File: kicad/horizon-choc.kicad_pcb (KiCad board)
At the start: 2 copper layers, 252 x 68 mm, 117 parts, among them SW1 SW_Push, SW10 SW_Push, SW11 SW_Push, SW12 SW_Push, SW13 SW_Push, SW14 SW_Push, SW15 SW_Push, SW16 SW_Push, SW17 SW_Push, SW18 SW_Push, SW19 SW_Push, SW2 SW_Push, SW20 SW_Push, SW21 SW_Push, SW22 SW_Push, SW23 SW_Push, SW24 SW_Push, SW25 SW_Push, SW26 SW_Push, SW27 SW_Push, SW28 SW_Push, SW29 SW_Push, SW3 SW_Push, SW30 SW_Push, SW31 SW_Push, SW32 SW_Push, SW33 SW_Push, SW34 SW_Push, SW35 SW_Push, SW36 SW_Push, SW37 SW_Push, SW38 SW_Push, SW39 SW_Push, SW4 SW_Push, SW40 SW_Push, SW41 SW_Push, SW42 SW_Push, SW43 SW_Push, SW44 SW_Push, SW45 SW_Push, SW46 SW_Push, SW47 SW_Push, SW48 SW_Push, SW49 SW_Push, SW5 SW_Push, SW50 SW_Push, SW51 SW_Push, SW52 SW_Push, SW6 SW_Push, SW7 SW_Push, SW8 SW_Push, SW9 SW_Push, U1 PRO-MICRO

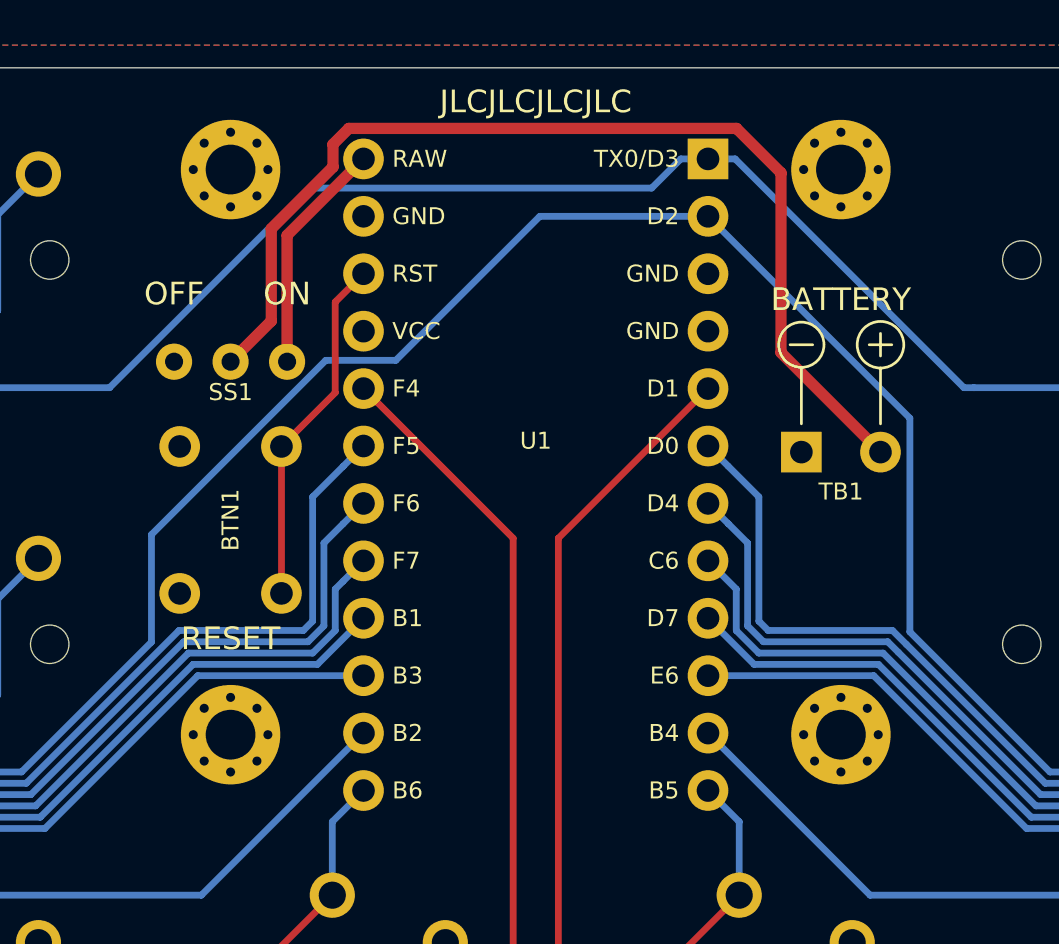
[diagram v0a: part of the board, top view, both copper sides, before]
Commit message: Update plate outlines. Remove battery from Choc design for now
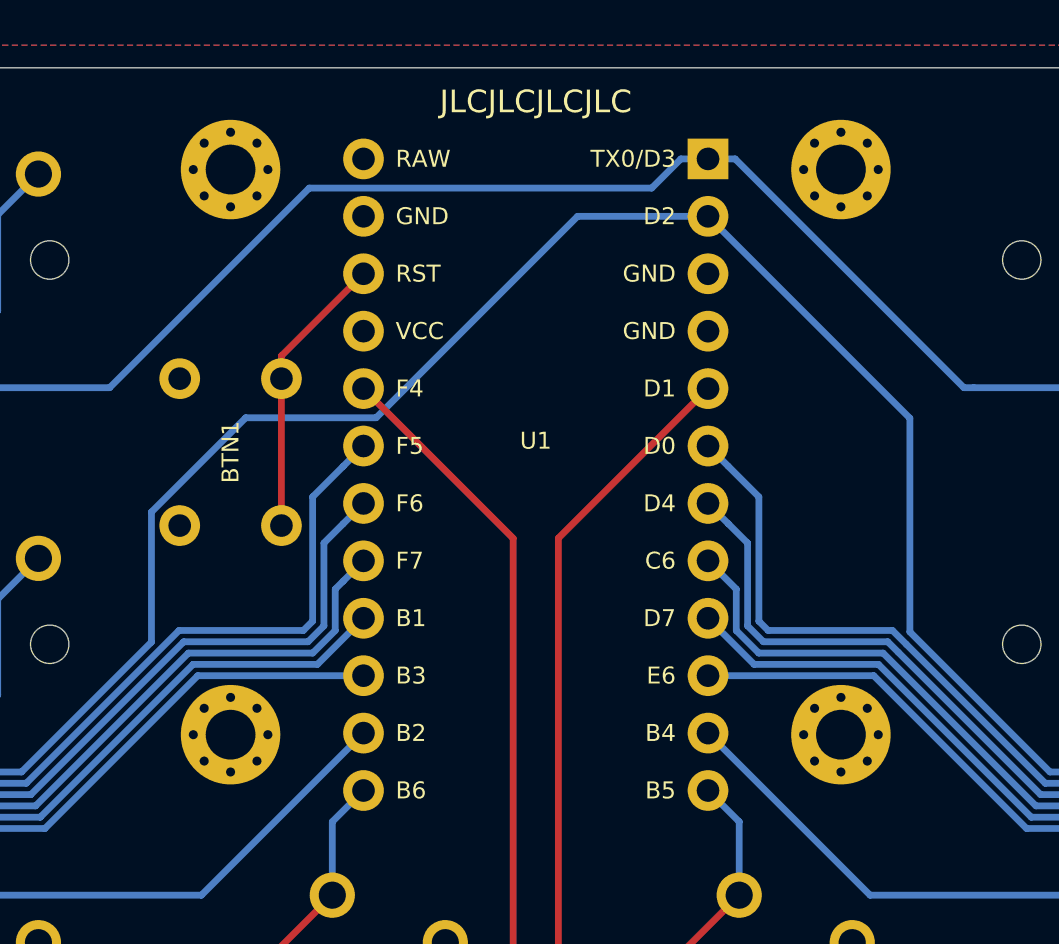
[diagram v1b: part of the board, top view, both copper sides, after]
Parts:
- removed SS1: POWER, horizon-footprints:SS12D00
- removed TB1: BATTERY, horizon-footprints:KF350-2P
- moved BTN1 3.00 mm to (188.5, 112.0)
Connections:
- U1 pad 24: RAW -> (no net)
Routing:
- net +BATT: track 46.6 -> 0.00 mm
- net RAW: track 10.4 -> 0.00 mm
- net RESET: track 15.6 -> 12.6 mm
- net ROW2: track 284.4 -> 285.0 mm
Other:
- board text removed: "BATTERY"
- board text removed: "OFF"
- board text removed: "ON"
- board text removed: "RESET"
